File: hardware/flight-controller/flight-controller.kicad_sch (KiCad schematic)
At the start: 0 parts

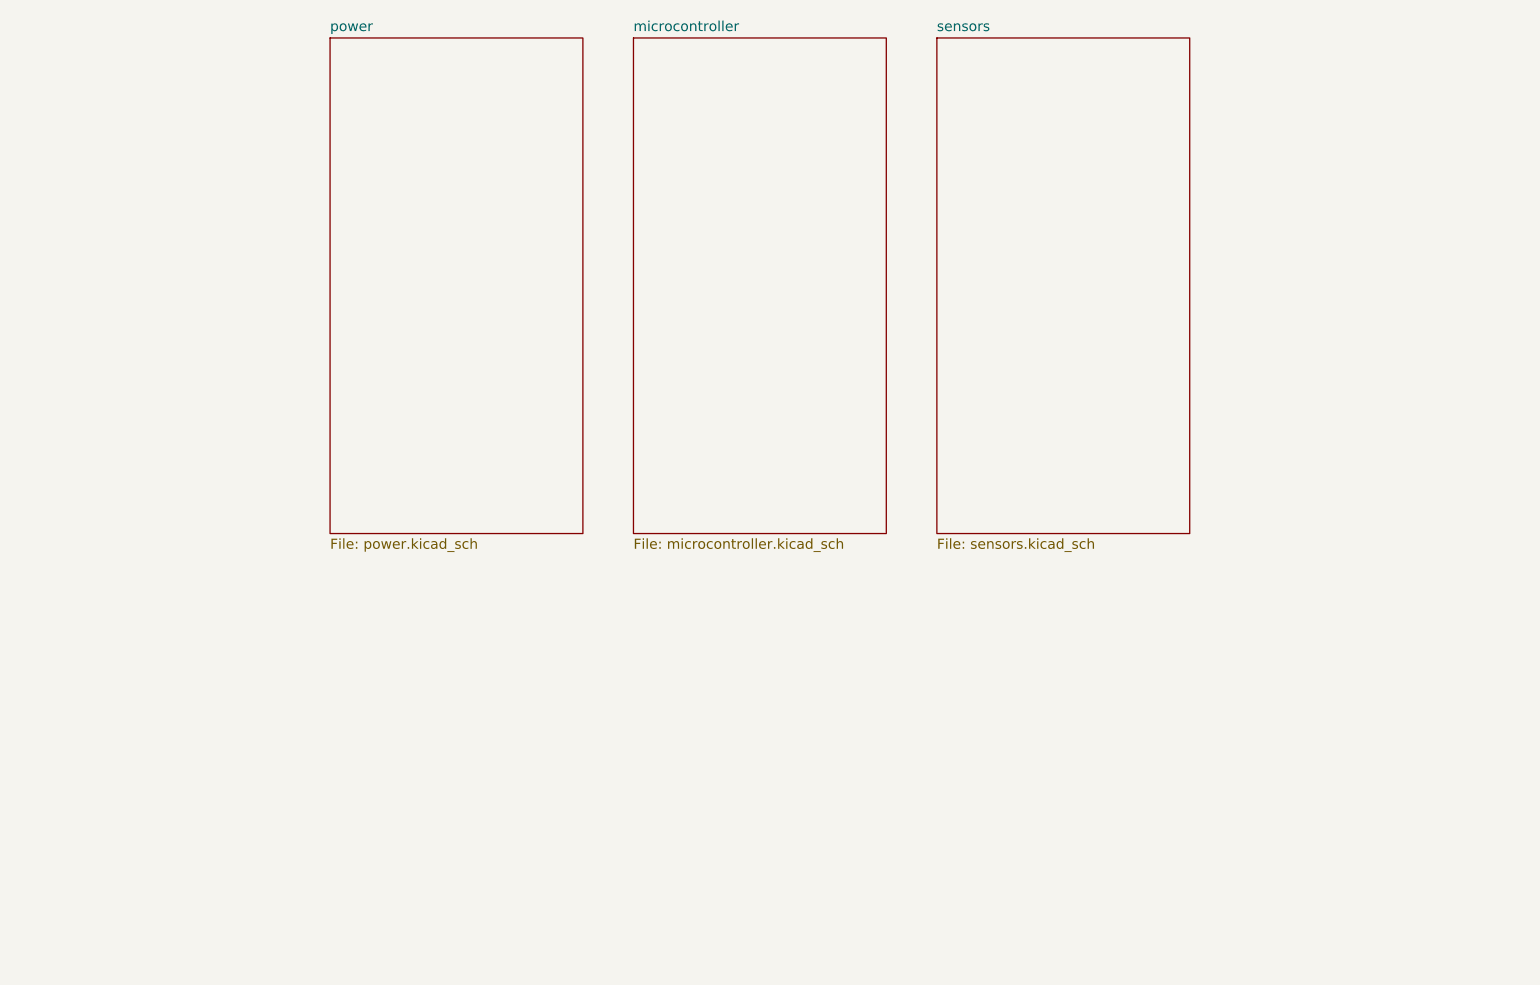
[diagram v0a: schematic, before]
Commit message: sensors, power, actuators, filters
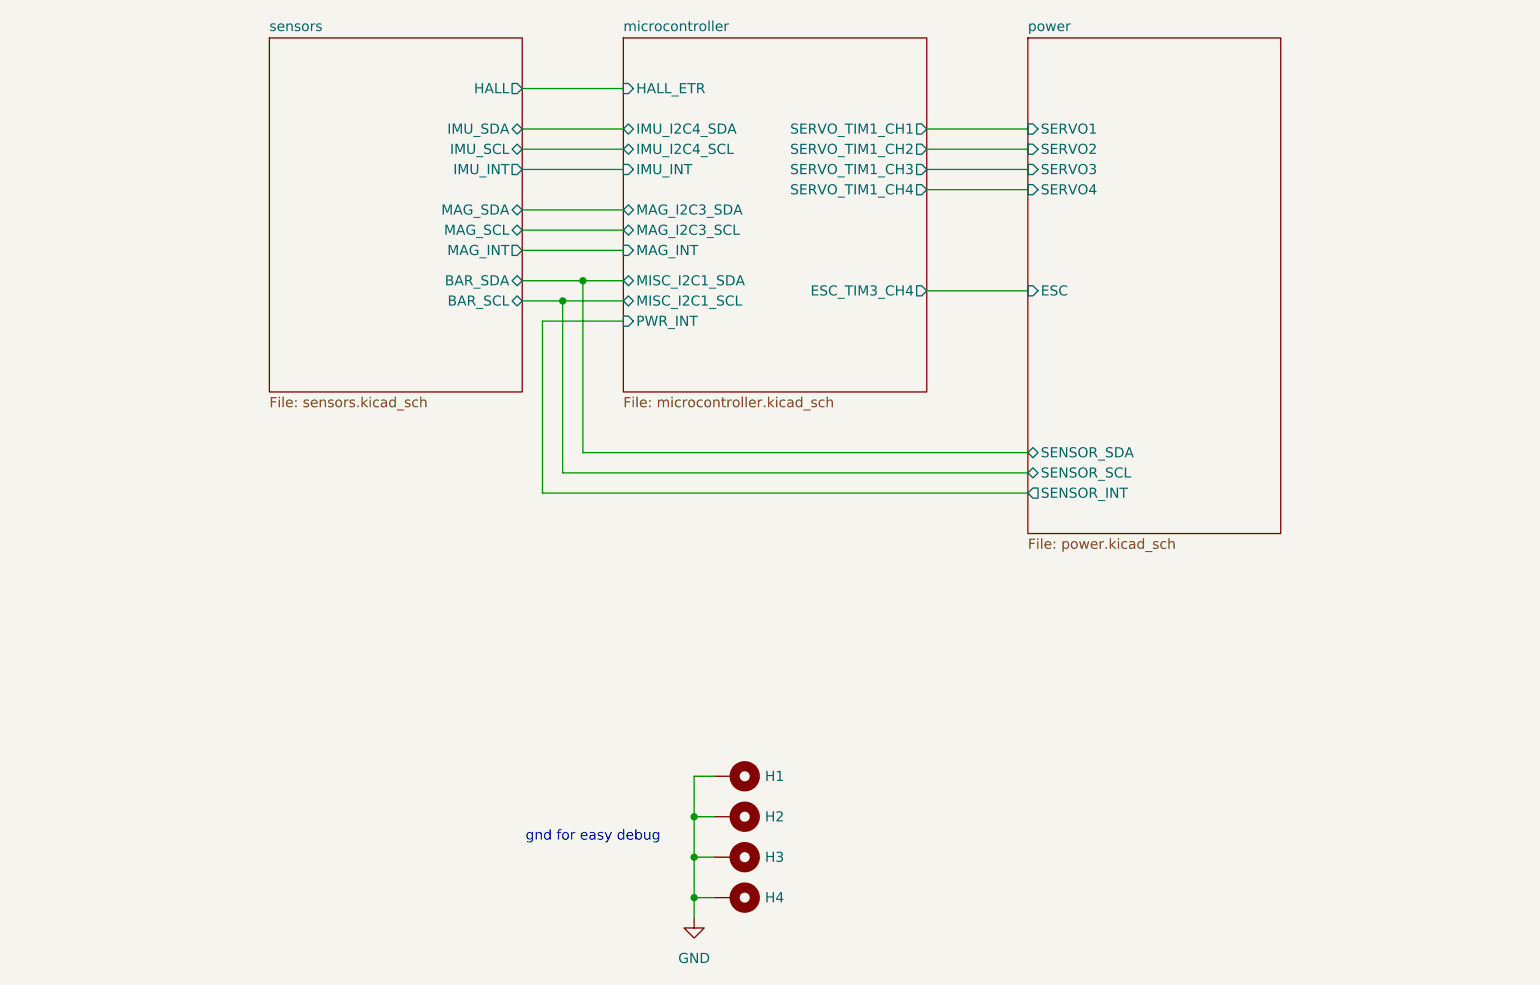
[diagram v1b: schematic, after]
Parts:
- added H1, H2, H3, H4: MountingHole_Pad, symbol Mechanical:MountingHole_Pad
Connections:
- new net GND: H1.1, H2.1, H3.1, H4.1
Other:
- sheet microcontroller ports: added ESC_TIM3_CH4, HALL_ETR, IMU_I2C4_SCL, IMU_I2C4_SDA, IMU_INT, MAG_I2C3_SCL, MAG_I2C3_SDA, MAG_INT, MISC_I2C1_SCL, MISC_I2C1_SDA, PWR_INT, SERVO_TIM1_CH1, SERVO_TIM1_CH2, SERVO_TIM1_CH3, SERVO_TIM1_CH4; removed none
- sheet power ports: added ESC, SENSOR_INT, SENSOR_SCL, SENSOR_SDA, SERVO1, SERVO2, SERVO3, SERVO4; removed none
- sheet sensors ports: added BAR_SCL, BAR_SDA, HALL, IMU_INT, IMU_SCL, IMU_SDA, MAG_INT, MAG_SCL, MAG_SDA; removed none
- note added: "gnd for easy debug"

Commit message: schematic cleanup
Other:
- added sheet actuators (actuators.kicad_sch)
- sheet microcontroller ports: added ESC, FLOW_CS, FLOW_INT, FLOW_MISO, FLOW_MOSI, FLOW_SCK, GPS_RX, GPS_TX, HALL, IMU_SCL, IMU_SDA, MAG_SCL, MAG_SDA, MISC_SCL, MISC_SDA, RANGE_ECHO, RANGE_TRIG, SERVO1, SERVO2, SERVO3, SERVO4; removed ESC_TIM3_CH4, HALL_ETR, IMU_I2C4_SCL, IMU_I2C4_SDA, MAG_I2C3_SCL, MAG_I2C3_SDA, MISC_I2C1_SCL, MISC_I2C1_SDA, SERVO_TIM1_CH1, SERVO_TIM1_CH2, SERVO_TIM1_CH3, SERVO_TIM1_CH4
- sheet power ports: added SHUNT_HIGH, SHUNT_LOW; removed ESC, SENSOR_INT, SENSOR_SCL, SENSOR_SDA, SERVO1, SERVO2, SERVO3, SERVO4
- sheet sensors ports: added FLOW_CS, FLOW_INT, FLOW_MISO, FLOW_MOSI, FLOW_SCK, GPS_RX, GPS_TX, HALL_VEL, PWR_INT, RANGE_ECHO, RANGE_TRIG, SCL, SDA, SHUNT_HIGH, SHUNT_LOW; removed BAR_SCL, BAR_SDA, HALL
- note added: "twisted"

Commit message: still working
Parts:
- removed H1, H2, H3, H4: MountingHole_Pad, symbol Mechanical:MountingHole_Pad
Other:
- removed sheet actuators
- added sheet connectors (connectors.kicad_sch)
- sheet microcontroller ports: added none; removed ESC, FLOW_CS, FLOW_INT, FLOW_MISO, FLOW_MOSI, FLOW_SCK, GPS_RX, GPS_TX, HALL, IMU_INT, IMU_SCL, IMU_SDA, MAG_INT, MAG_SCL, MAG_SDA, MISC_SCL, MISC_SDA, PWR_INT, RANGE_ECHO, RANGE_TRIG, SERVO1, SERVO2, SERVO3, SERVO4
- sheet power ports: added none; removed SHUNT_HIGH, SHUNT_LOW
- sheet sensors ports: added none; removed FLOW_CS, FLOW_INT, FLOW_MISO, FLOW_MOSI, FLOW_SCK, GPS_RX, GPS_TX, HALL_VEL, IMU_INT, IMU_SCL, IMU_SDA, MAG_INT, MAG_SCL, MAG_SDA, PWR_INT, RANGE_ECHO, RANGE_TRIG, SCL, SDA, SHUNT_HIGH, SHUNT_LOW
- note removed: "gnd for easy debug"
- note removed: "twisted"

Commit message: generate schematic in pdf
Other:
- title: UAV TVC Goose Flight Controller -> UAV TVC Goose II: Flight Controller
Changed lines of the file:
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@@
 	(paper "A4")
 	(title_block
-		(title "UAV TVC Goose Flight Controller")
+		(title "UAV TVC Goose II: Flight Controller")
 		(date "2024-08-05")
 		(rev "V2.1")
